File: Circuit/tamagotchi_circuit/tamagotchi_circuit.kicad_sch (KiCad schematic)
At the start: 5 parts

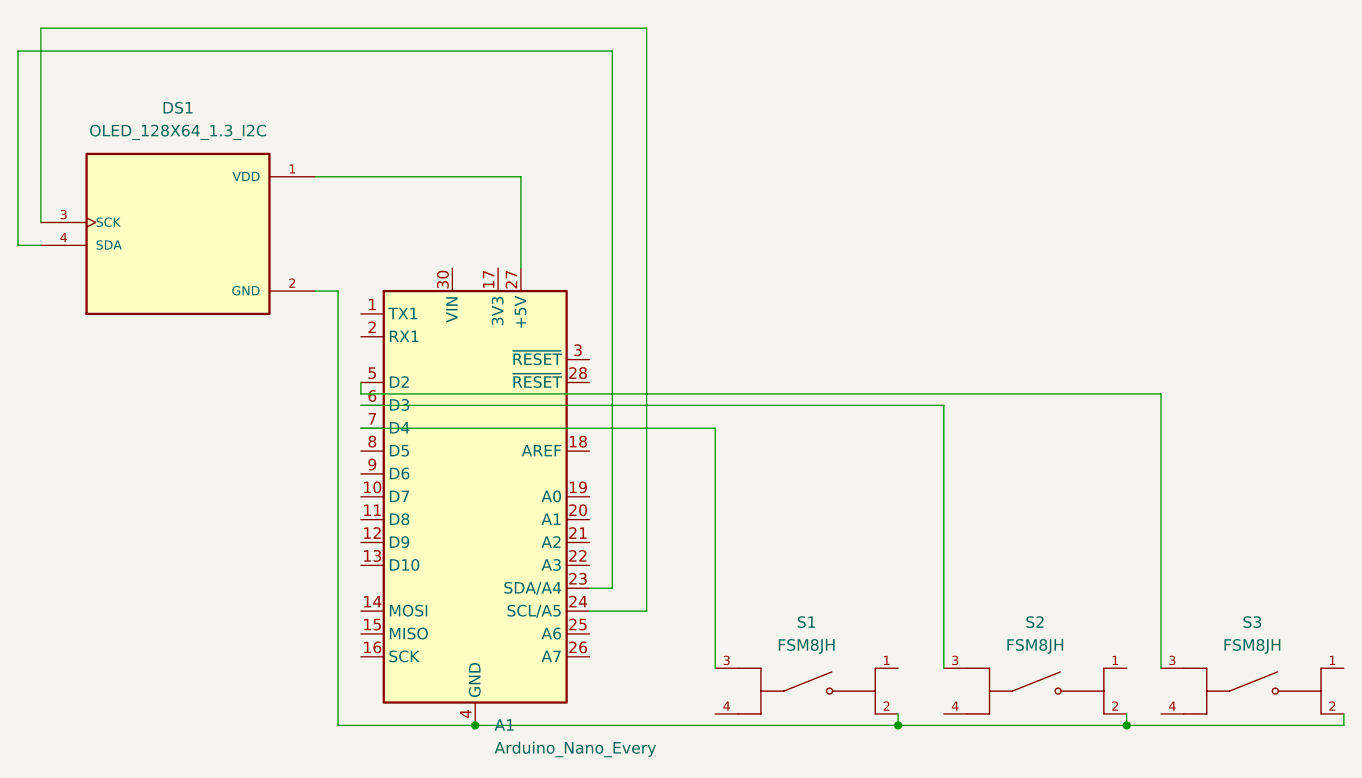
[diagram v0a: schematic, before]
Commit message: Added Readme Journala and 3D Model Images
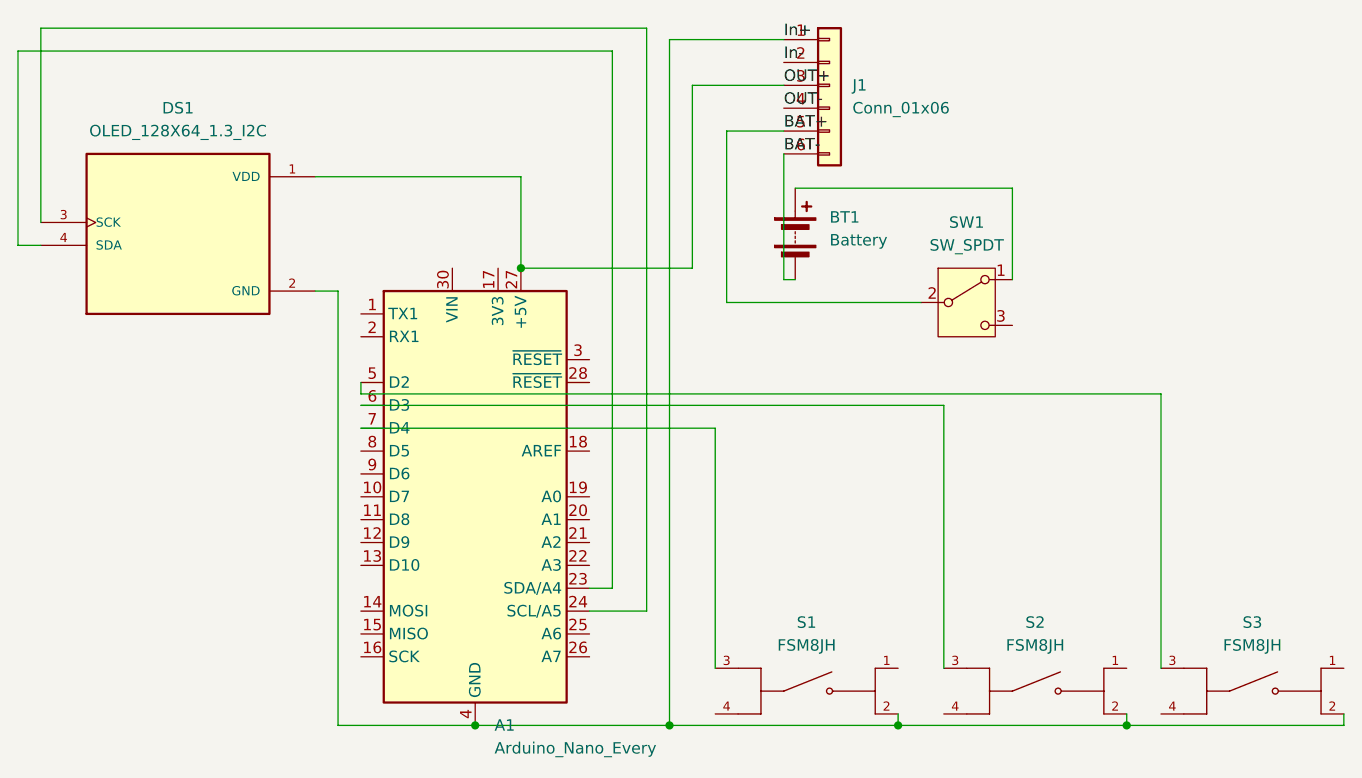
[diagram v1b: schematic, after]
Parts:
- added BT1: Battery, symbol Device:Battery
- added J1: Conn_01x06, symbol Connector_Generic:Conn_01x06
- added SW1: SW_SPDT, symbol Switch:SW_SPDT
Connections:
- net OUT+: now reaches A1.27 (+5V), DS1.1 (VDD)
- net OUT+: now also J1.3 (Pin_3)
- net In+: now reaches A1.29 (GND), A1.4 (GND), DS1.2 (GND), S1.2, S2.2, S3.2
- net In+: now also J1.1 (Pin_1)
- new net: BT1.1 (+), SW1.1 (A)
- new net BAT+: J1.5 (Pin_5), SW1.2 (B)
- new net BAT-: BT1.2 (-), J1.6 (Pin_6)
- new net In-: J1.2 (Pin_2)
- new net OUT-: J1.4 (Pin_4)

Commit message: Update circuit schematic footprints, add new images, and enhance documentation
- Updated footprints for components in the tamagotchi circuit schematic.
- Added new images including Front.PNG, QRCODE.png, QR_TRANSPARENT.png, arduino_transparent.png, screen_Front_transparent.png, and shell.png.
- Updated the README.md to include a section for the shell image.
- Added new zine files: Tamagotchi Zine.pdf and Tamagotchi Zine.png.
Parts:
- BT1: footprint (none) -> Battery:Battery_Panasonic_CR1025-VSK_Vertical_CircularHoles
- J1: footprint (none) -> TP4056-18650-master:TP4056-18650
- SW1: footprint (none) -> EG1218:SW_EG1218
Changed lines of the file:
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@@
 			)
 		)
-		(property "Footprint" ""
+		(property "Footprint" "EG1218:SW_EG1218"
 			(at 167.64 77.47 0)
 			(effects
@@
 			)
 		)
-		(property "Footprint" ""
+		(property "Footprint" "Battery:Battery_Panasonic_CR1025-VSK_Vertical_CircularHoles"
 			(at 148.59 68.326 90)
 			(effects
@@
 			)
 		)
-		(property "Footprint" ""
+		(property "Footprint" "TP4056-18650-master:TP4056-18650"
 			(at 152.4 53.34 0)
 			(effects
